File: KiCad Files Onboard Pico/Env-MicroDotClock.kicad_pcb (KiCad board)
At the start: 2 copper layers, 90 x 65.2 mm, 57 parts, among them IC1 IS31FL3730-QFLS2-TR, IC2 IS31FL3730-QFLS2-TR, IC3 IS31FL3730-QFLS2-TR, IC4 IS31FL3730-QFLS2-TR, J1 Conn_01x06_Pin, J2 GT-USB-7051, M1 Dip-14 Socket, M2 Dip-14 Socket, M3 Dip-14 Socket, M4 Dip-14 Socket, M5 Dip-14 Socket, M6 Dip-14 Socket, M7 Dip-14 Socket, M8 Dip-14 Socket, SW1 SW_SPST, SW2 SW_SPST, SW3 SW_SPST, SW4 SW_SPST, SW5 SW_SPST, SW6 SW_SPST, U1 Raspberry Pi Pico, U3 DS3231M

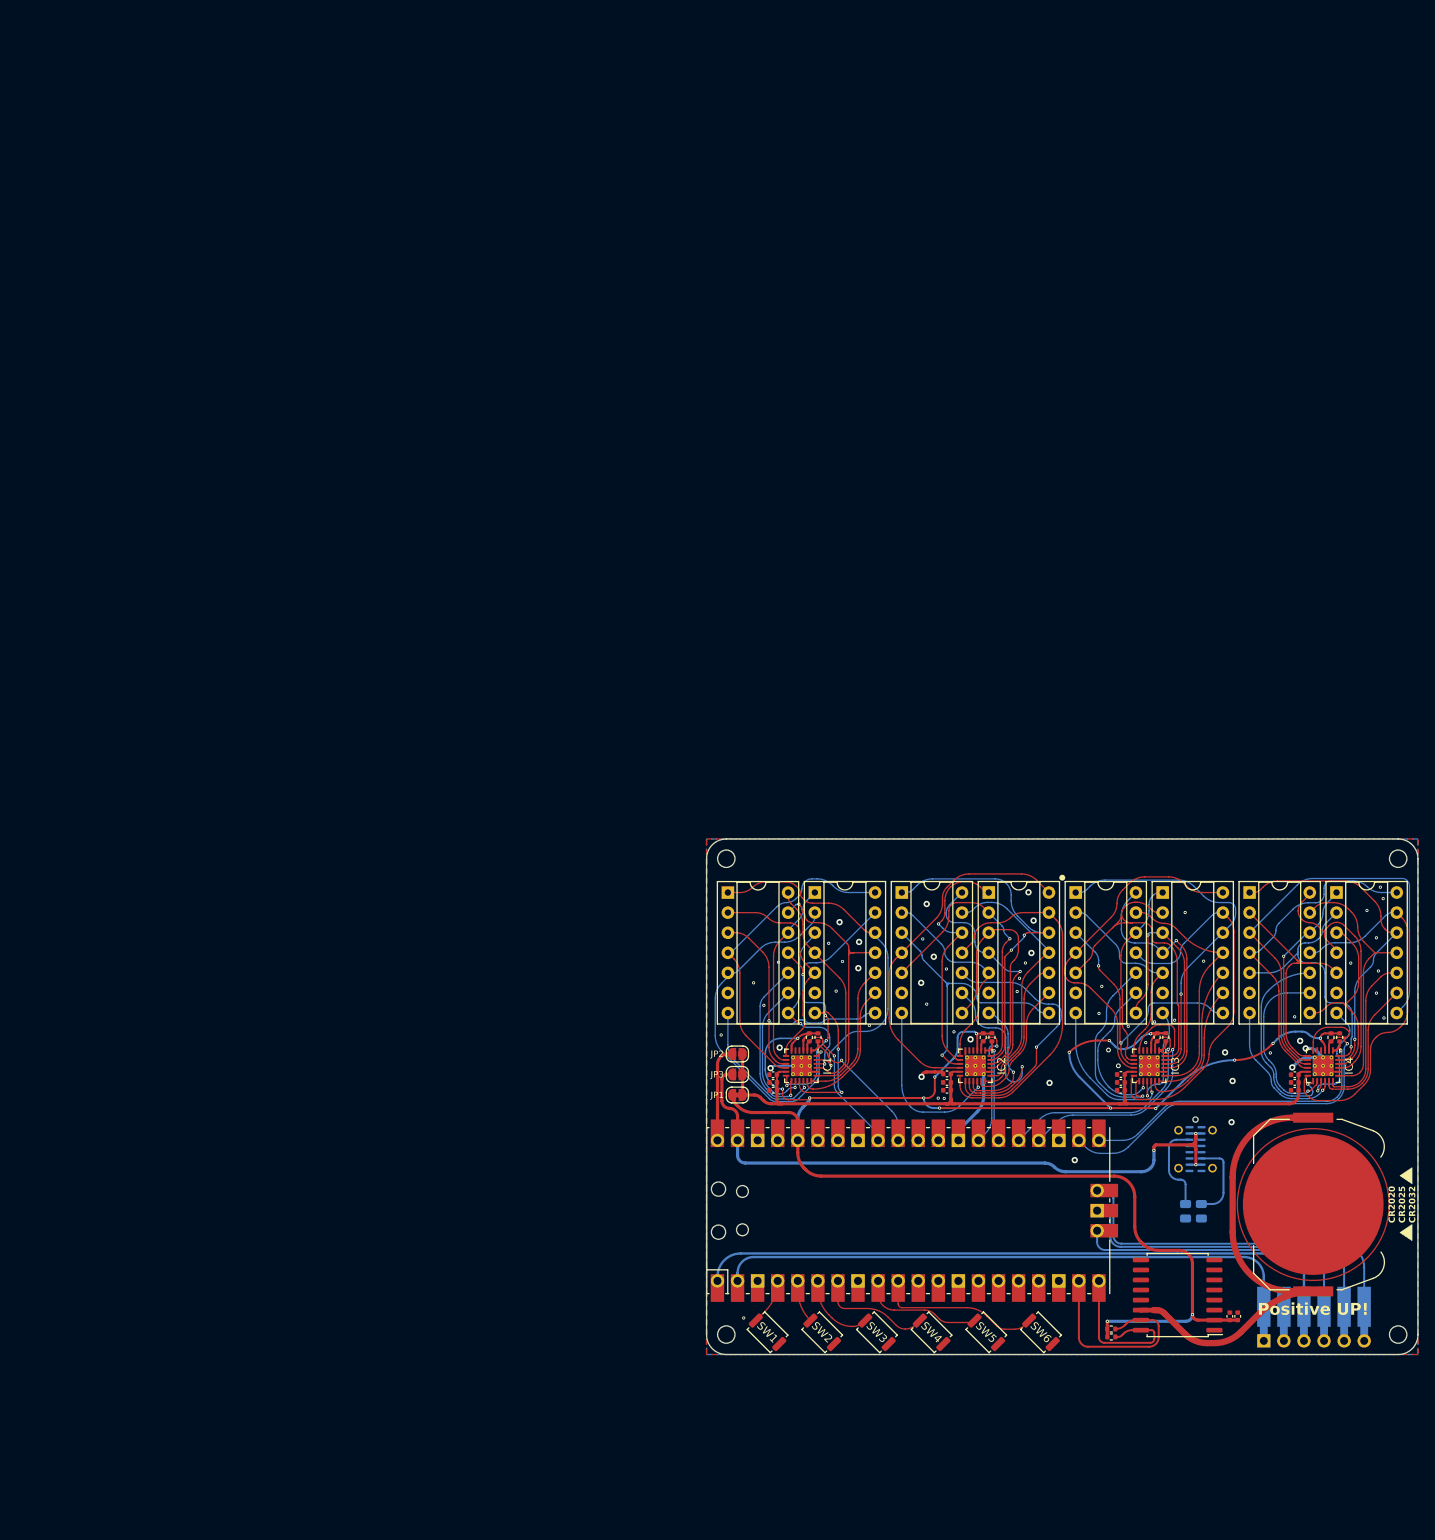
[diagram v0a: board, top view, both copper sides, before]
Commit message: Added onboard pico
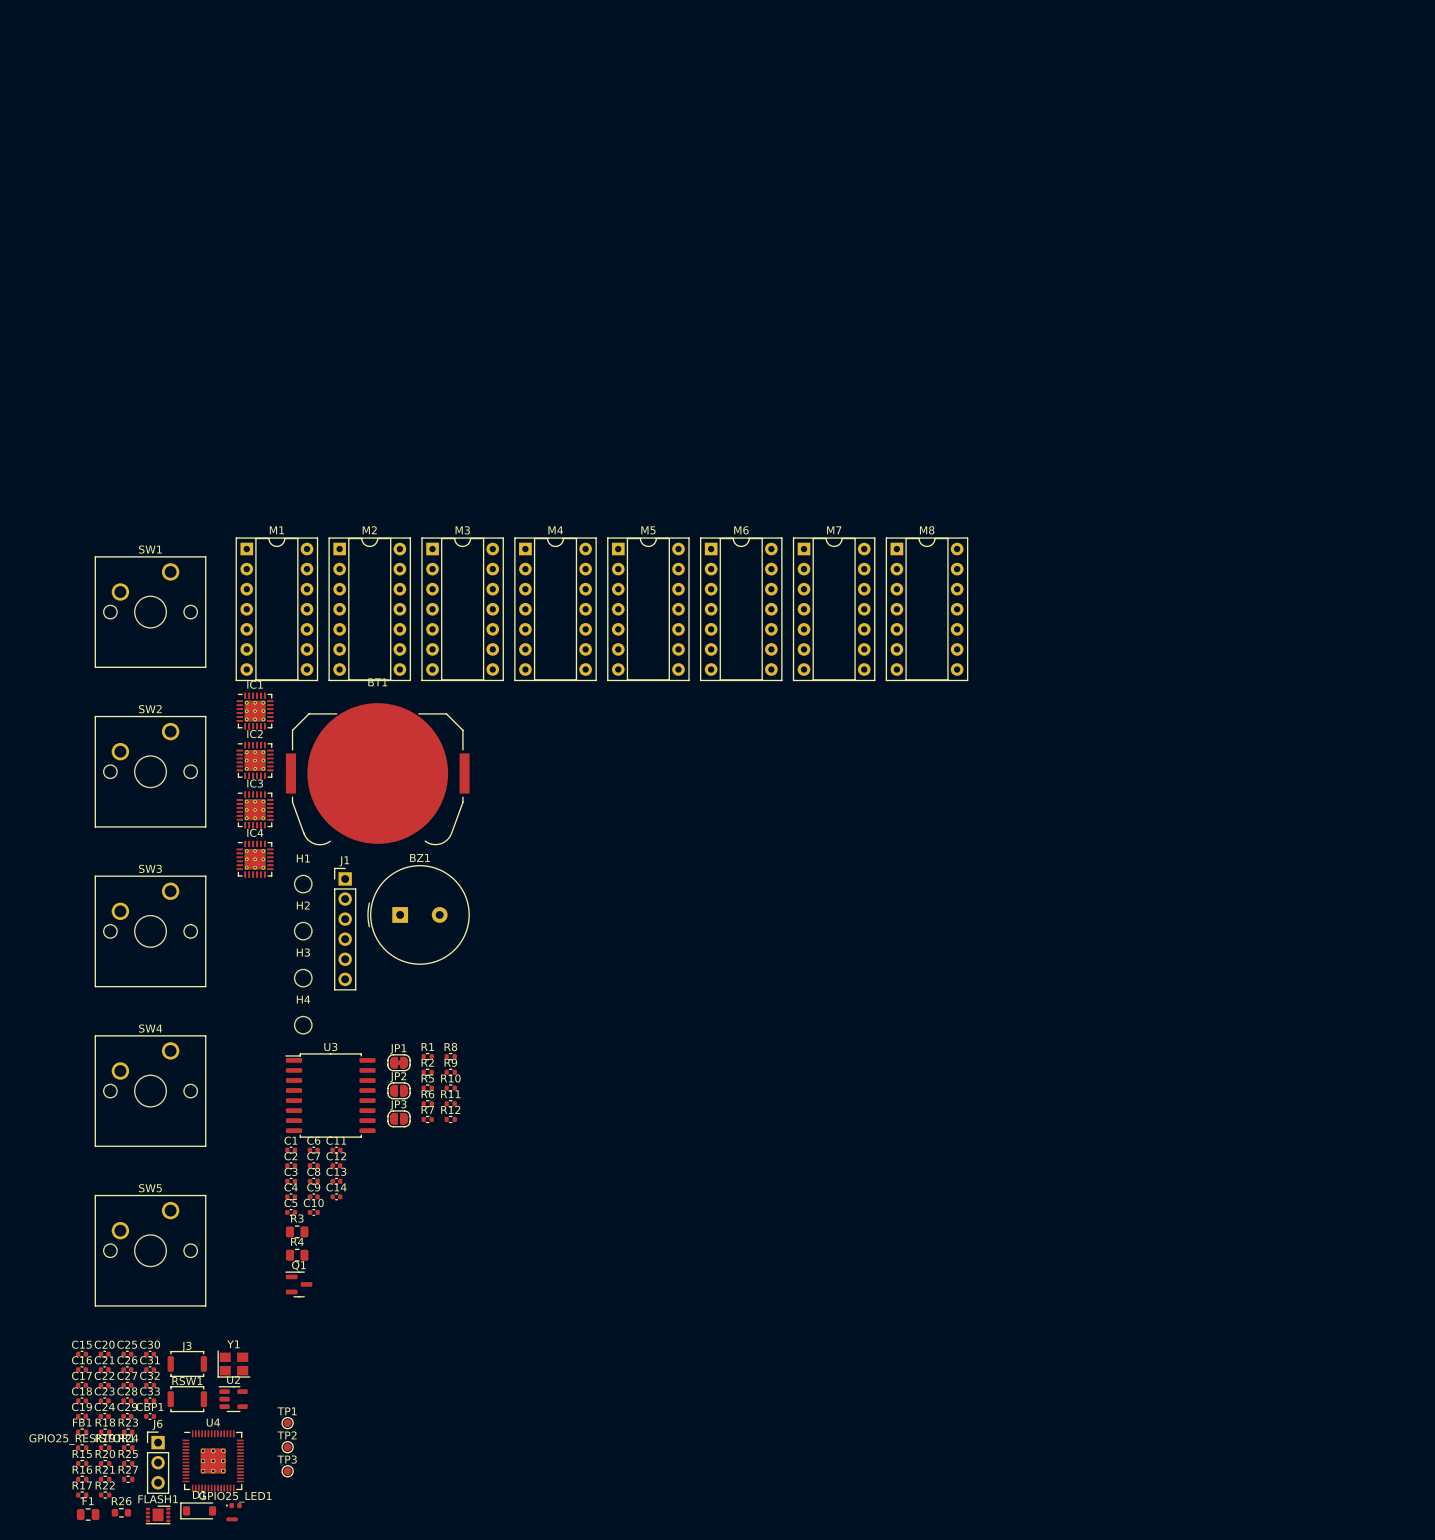
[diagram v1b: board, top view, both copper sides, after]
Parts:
- removed G***: LOGO, LOGO
- removed J2: GT-USB-7051, Connector_USB:USB_C_Receptacle_G-Switch_GT-USB-7051x
- removed R13, R14: 5.1K 0805, Resistor_SMD:R_0805_2012Metric
- removed SW6: SW_SPST, Button_Switch_SMD:SW_Push_SPST_NO_Alps_SKRK
- removed U1: Raspberry Pi Pico, MCU_RaspberryPi_and_Boards:RPi_Pico_SMD_TH
- added BZ1: Buzzer 12.2Mm, Buzzer_Beeper:Buzzer_TDK_PS1240P02BT_D12.2mm_H6.5mm, F.Cu at (46.2, 67.1)
- added C15: 0.1uf 0402, Capacitor_SMD:C_0402_1005Metric, F.Cu at (5.99, 122.7)
- added C16: 22pf 0402, Capacitor_SMD:C_0402_1005Metric, F.Cu at (5.99, 124.7)
- added C17: 22pf 0402, Capacitor_SMD:C_0402_1005Metric, F.Cu at (5.99, 126.6)
- added C18: 100nf 0402, Capacitor_SMD:C_0402_1005Metric, F.Cu at (5.99, 128.6)
- added C19: 10uf 0402, Capacitor_SMD:C_0402_1005Metric, F.Cu at (5.99, 130.6)
- added C20: 10uf 0402, Capacitor_SMD:C_0402_1005Metric, F.Cu at (8.86, 122.7)
- added C21: 100nf 0402, Capacitor_SMD:C_0402_1005Metric, F.Cu at (8.86, 124.7)
- added C22: 100nf 0402, Capacitor_SMD:C_0402_1005Metric, F.Cu at (8.86, 126.6)
- added C23: 1uf 0402, Capacitor_SMD:C_0402_1005Metric, F.Cu at (8.86, 128.6)
- added C24: 100nf 0402, Capacitor_SMD:C_0402_1005Metric, F.Cu at (8.86, 130.6)
- added C25: 2.2uF 0402, Capacitor_SMD:C_0402_1005Metric, F.Cu at (11.7, 122.7)
- added C26: 100nf 0402, Capacitor_SMD:C_0402_1005Metric, F.Cu at (11.7, 124.7)
- added C27: 100nf 0402, Capacitor_SMD:C_0402_1005Metric, F.Cu at (11.7, 126.6)
- added C28: 100nf 0402, Capacitor_SMD:C_0402_1005Metric, F.Cu at (11.7, 128.6)
- added C29: 100nf 0402, Capacitor_SMD:C_0402_1005Metric, F.Cu at (11.7, 130.6)
- added C30: 100nf 0402, Capacitor_SMD:C_0402_1005Metric, F.Cu at (14.6, 122.7)
- added C31: 100nf 0402, Capacitor_SMD:C_0402_1005Metric, F.Cu at (14.6, 124.7)
- added C32: 2.2uF 0402, Capacitor_SMD:C_0402_1005Metric, F.Cu at (14.6, 126.6)
- added C33: 10uf 0402, Capacitor_SMD:C_0402_1005Metric, F.Cu at (14.6, 128.6)
- added CBP1: 10uf 0402, Capacitor_SMD:C_0402_1005Metric, F.Cu at (14.6, 130.6)
- added D1: 1N4002W, Diode_SMD:D_SOD-123, F.Cu at (20.9, 142.5)
- added F1: 0805L050WR, Fuse:Fuse_0805_2012Metric, F.Cu at (6.76, 143.0)
- added FB1: FerriteBead 0402, Resistor_SMD:R_0402_1005Metric, F.Cu at (6.01, 132.5)
- added FLASH1: W25Q16JVUXIQ, Package_SON:SON-8-1EP_3x2mm_P0.5mm_EP1.4x1.6mm, F.Cu at (15.6, 143.0)
- added GPIO25_LED1: LED_0402, LED_SMD:LED_0402_1005Metric, F.Cu at (25.4, 141.8)
- added GPIO25_RESISTOR1: 470 0402, Resistor_SMD:R_0402_1005Metric, F.Cu at (6.01, 134.5)
- added J3: Button, Button_Switch_SMD:SW_Push_SPST_NO_Alps_SKRK, F.Cu at (19.3, 123.9)
- added J6: Conn_01x03_Male, Connector_PinHeader_2.54mm:PinHeader_1x03_P2.54mm_Vertical, F.Cu at (15.6, 133.9)
- added NT1: NetTie_2, NetTie:NetTie-2_SMD_Pad0.5mm, F.Cu at (25.0, 143.6)
- added Q1: 2SC1815, Package_TO_SOT_SMD:SOT-23, F.Cu at (33.5, 113.9)
- added R15: 5.1K 0402, Resistor_SMD:R_0402_1005Metric, F.Cu at (6.01, 136.5)
- added R16: 5.1K 0402, Resistor_SMD:R_0402_1005Metric, F.Cu at (6.01, 138.5)
- added R17: 220 0402, Resistor_SMD:R_0402_1005Metric, F.Cu at (6.01, 140.5)
- added R18: 1K 0402, Resistor_SMD:R_0402_1005Metric, F.Cu at (8.92, 132.5)
- added R19: 5.6K 0402, Resistor_SMD:R_0402_1005Metric, F.Cu at (8.92, 134.5)
- added R20: 10K 0402, Resistor_SMD:R_0402_1005Metric, F.Cu at (8.92, 136.5)
- added R21: 10K 0402, Resistor_SMD:R_0402_1005Metric, F.Cu at (8.92, 138.5)
- added R22: 100K 0402, Resistor_SMD:R_0402_1005Metric, F.Cu at (8.92, 140.5)
- added R23: 1K 0402, Resistor_SMD:R_0402_1005Metric, F.Cu at (11.8, 132.5)
- added R24: 27r 0402 resistor, Resistor_SMD:R_0402_1005Metric, F.Cu at (11.8, 134.5)
- added R25: 27r 0402 resistor, Resistor_SMD:R_0402_1005Metric, F.Cu at (11.8, 136.5)
- added R26: 200 0603, Resistor_SMD:R_0603_1608Metric, F.Cu at (11.0, 142.8)
- added R27: 1 0402, Resistor_SMD:R_0402_1005Metric, F.Cu at (11.8, 138.5)
- added R3: 0805 1K, Resistor_SMD:R_0805_2012Metric, F.Cu at (33.2, 107.2)
- added R4: 0805 1K, Resistor_SMD:R_0805_2012Metric, F.Cu at (33.2, 110.2)
- added RSW1: TSA343G00-250J2, Button_Switch_SMD:SW_Push_SPST_NO_Alps_SKRK, F.Cu at (19.3, 128.4)
- added TP1: TestPoint, TestPoint:TestPoint_Pad_D1.0mm, F.Cu at (32.0, 131.4)
- added TP2: TestPoint, TestPoint:TestPoint_Pad_D1.0mm, F.Cu at (32.0, 134.4)
- added TP3: TestPoint, TestPoint:TestPoint_Pad_D1.0mm, F.Cu at (32.0, 137.5)
- added U2: SOT-23-5 5.5V 3.3V 500mA, Package_TO_SOT_SMD:SOT-23-5, F.Cu at (25.2, 128.4)
- added U4: RP2040, MCU_RaspberryPi_and_Boards:RP2040-QFN-56, F.Cu at (22.6, 136.2)
- added Y1: 3225_4P 12MHz, Crystal:Crystal_SMD_3225-4Pin_3.2x2.5mm, F.Cu at (25.2, 123.9)
- J1: moved to F.Cu
- SW1, SW2, SW3, SW4, SW5: value SW_SPST -> SW_Push; footprint Button_Switch_SMD:SW_Push_SPST_NO_Alps_SKRK -> Button_Switch_Keyboard:SW_Cherry_MX_1.00u_PCB
- moved H1 149.8 mm to (34.0, 63.2)
- moved H3 139.3 mm to (34.0, 75.1)
- moved IC4 137.6 mm to (27.9, 60.1), turned to 0 degrees
- moved BT1 130.3 mm to (43.4, 49.2), turned to 0 degrees
- moved J1 130.1 mm to (39.3, 62.6), turned to 0 degrees
- moved C8 124.7 mm to (35.3, 100.8), turned to 0 degrees
- moved C7 124.6 mm to (35.3, 98.8), turned to 0 degrees
- moved SW1 122.3 mm to (17.2, 23.7), turned to 0 degrees
- moved C12 121.6 mm to (38.2, 98.8), turned to 0 degrees
- moved IC3 117.7 mm to (27.9, 53.8), turned to 0 degrees
- moved C10 117.6 mm to (35.3, 104.8), turned to 0 degrees
- moved C9 116.9 mm to (35.3, 102.8), turned to 0 degrees
- moved R5 115.6 mm to (49.7, 89.0), turned to 0 degrees
- moved R6 114.6 mm to (49.7, 91.0), turned to 0 degrees
- moved SW2 112.1 mm to (17.2, 43.9), turned to 0 degrees
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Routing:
- net +3V3: track 244.1 -> 0.00 mm, vias 17 -> 0
- net VCC: track 100.3 -> 0.00 mm
- net TX: track 86.2 -> 0.00 mm
- net VDD: track 82.8 -> 0.00 mm, vias 3 -> 0
- net RX: track 78.1 -> 0.00 mm
- net Net-(BT1-+): track 60.6 -> 0.00 mm
- net IC4R3: track 59.9 -> 0.00 mm
- net I2C4_SCL: track 55.2 -> 0.00 mm, vias 1 -> 0
- net SWDIO: track 50.5 -> 0.00 mm
- net IC3R5: track 49.2 -> 0.00 mm
- net IC4R5: track 48.6 -> 0.00 mm
- net IC2R5: track 47.8 -> 0.00 mm
- net IC2R4: track 45.7 -> 0.00 mm
- net IC1C2: track 45.5 -> 0.00 mm, vias 1 -> 0
- net IC1C1: track 45.4 -> 0.00 mm, vias 1 -> 0
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- removed copper zone on B.Cu, net GND
- removed copper zone on F.Cu, net GND
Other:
- board outline removed
- rule pad_to_mask_clearance: 0.051 -> 0
- board text removed: "AUX USB PWR ONLY"
- board text removed: "CR2020 CR2025 CR2032"
- board text removed: "Positive UP!"
- board text removed: "RX GND TX SWCLK GND SWDIO"
- board text removed: "env"
- board text removed: "https://GitHub.com/Envious-Data/Env-OpenClock"

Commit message: for cat
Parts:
- added U1: Si7021-A20, Package_DFN_QFN:DFN-6-1EP_3x3mm_P1mm_EP1.5x2.4mm, F.Cu at (139.4, 97.8)
- added USB1: TYPE-C-31-M-12, Connector_USB:USB_C_Receptacle_HRO_TYPE-C-31-M-12, F.Cu at (66.0, 118.4)
- moved Q1 118.7 mm to (147.8, 82.0)
- moved SW5 116.8 mm to (131.3, 129.4)
- moved R10 115.3 mm to (167.9, 87.8)
- moved R11 115.3 mm to (167.9, 89.8)
- moved R12 115.3 mm to (167.9, 91.8)
- moved R8 115.3 mm to (167.9, 83.8)
- moved R9 115.3 mm to (167.9, 85.8)
- moved SW1 110.8 mm to (50.5, 129.4)
- moved Y1 108.1 mm to (132.1, 107.8)
- moved BZ1 107.0 mm to (152.0, 51.0)
- moved C1 107.0 mm to (138.2, 80.8)
- moved C10 107.0 mm to (141.1, 88.6)
- moved C2 107.0 mm to (138.2, 82.7)
- moved C3 107.0 mm to (138.2, 84.7)
- moved C4 107.0 mm to (138.2, 86.7)
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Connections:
- IC1 pad 1: I2C1_SDA -> GPIO0
- IC1 pad 2: I2C1_SCL -> GPIO1
- IC2 pad 1: I2C2_SDA -> GPIO4
- IC2 pad 2: I2C2_SCL -> GPIO5
- IC3 pad 1: I2C3_SDA -> GPIO8
- IC3 pad 2: I2C3_SCL -> GPIO9
- IC3 pad 6: I2C3_SDA -> GPIO8
- IC4 pad 1: I2C4_SDA -> GPIO12
- IC4 pad 2: I2C4_SCL -> GPIO13
- IC4 pad 6: I2C4_SCL -> GPIO13
- R1 pad 2: RTC_SCL -> GPIO7
- R10 pad 2: I2C1_SCL -> GPIO1
- R11 pad 2: I2C2_SDA -> GPIO4
- R12 pad 2: I2C2_SCL -> GPIO5
- R2 pad 2: RTC_SDA -> GPIO6
- R5 pad 2: I2C4_SDA -> GPIO12
- R6 pad 2: I2C4_SCL -> GPIO13
- R7 pad 2: I2C3_SDA -> GPIO8
- R8 pad 2: I2C3_SCL -> GPIO9
- R9 pad 2: I2C1_SDA -> GPIO0
- U3 pad 15: RTC_SDA -> GPIO6
- U3 pad 16: RTC_SCL -> GPIO7

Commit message: Commit for night, progess on onboard RP2040
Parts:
- removed J6: Conn_01x03_Male, Connector_PinHeader_2.54mm:PinHeader_1x03_P2.54mm_Vertical
- JP1, JP2, JP3, TP1, TP2, TP3: moved to B.Cu
- moved R10 145.9 mm to (29.5, 41.5)
- moved R9 145.7 mm to (29.5, 40.3)
- moved JP1 144.0 mm to (16.1, 21.5), turned to 180 degrees
- moved JP2 144.0 mm to (16.1, 25.1), turned to 180 degrees
- moved JP3 144.0 mm to (16.1, 28.6), turned to 180 degrees
- moved R17 136.4 mm to (118.1, 45.9), turned to 180 degrees
- moved J1 131.8 mm to (16.0, 73.4)
- moved H3 127.8 mm to (16.0, 91.0)
- moved BT1 127.7 mm to (24.0, 58.5), turned to -90 degrees
- moved H1 127.6 mm to (16.0, 16.0)
- moved R16 126.4 mm to (111.6, 51.7)
- moved R12 125.8 mm to (52.6, 41.5)
- moved R11 125.4 mm to (52.6, 40.4)
- moved C15 125.0 mm to (118.1, 47.0)
- moved R15 123.3 mm to (111.6, 54.7)
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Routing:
- added copper zone on B.Cu, net GND
- added copper zone on F.Cu, net GND
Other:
- board outline added: 110 x 80 mm
